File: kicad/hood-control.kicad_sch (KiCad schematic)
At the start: 32 parts, among them J1 Hoodcontrol, J2 FTDI Serial Flash, J3 Frontpanel, J4 Reset, J5 Flash/Run, J6 PWR_IN, SW1 Reset, SW2 Flash, U1 ESP-12E, U2 4050, U3 74HCT08, U4 Stepdown 3.3V

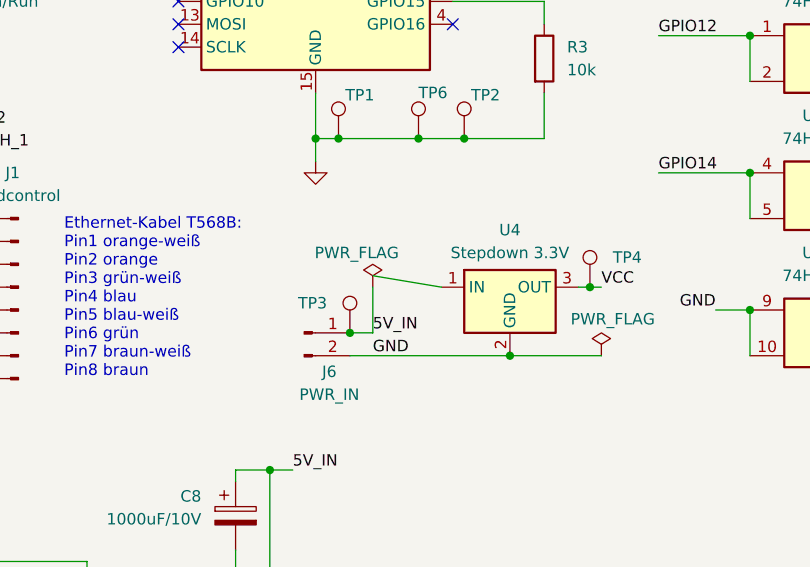
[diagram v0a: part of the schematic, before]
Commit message: Connect U4 VIN to the 5V input rail
The wire meant to feed the stepdown ran from (90.17, 92.71) diagonally
to U4 pin 1, missing the PWR_FLAG node by 1.27 mm. The converter input
was therefore on no net at all - ERC reported both "Pin not connected"
and "Input Power pin not driven", and the board would have been
fabricated with the 3.3 V supply dangling.

Replaced by a horizontal wire with a junction on the flag node. /5V_IN
now reads C5.1, C8.1, J6.1, TP3.1, U3.14, U4.1 and ERC is clean.

Co-Authored-By: Claude Opus 5 <noreply@anthropic.com>
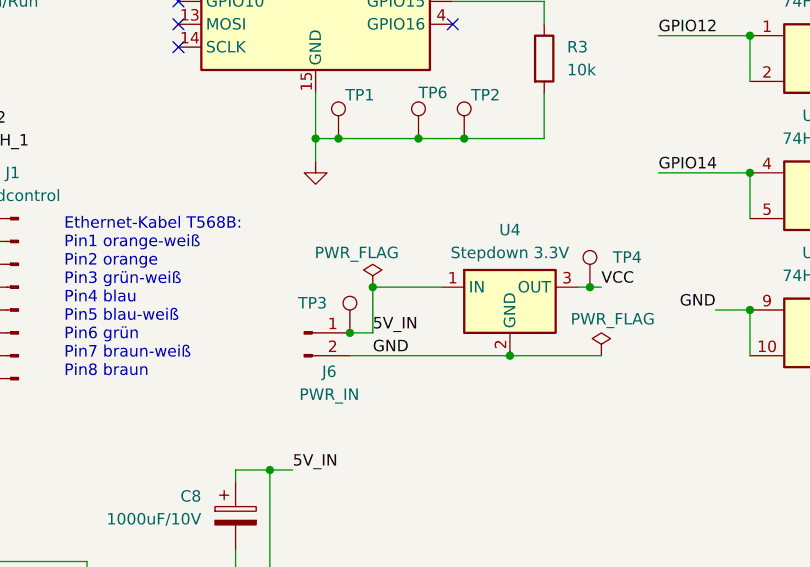
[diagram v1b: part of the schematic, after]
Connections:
- net 5V_IN: now also U4.1 (IN)
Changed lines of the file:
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@@
+	)
+	(junction
+		(at 90.17 93.98)
+		(diameter 0)
+		(color 0 0 0 0)
 	)
 	(junction
@@
 	(wire
 		(pts
+			(xy 90.17 93.98) (xy 97.79 93.98)
+		)
+		(stroke
+			(width 0)
+			(type default)
+		)
+	)
+	(wire
+		(pts
 			(xy 22.86 53.34) (xy 22.86 60.96)
 		)
@@
 		)
 		(stroke
-			(width 0)
-			(type default)
-		)
-	)
-	(wire
-		(pts
-			(xy 90.17 92.71) (xy 97.79 93.98)
-		)
-		(stroke
